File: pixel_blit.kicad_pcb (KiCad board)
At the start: 4 copper layers, 197.5 x 122 mm, 269 parts, among them CN1 PJ-3059-B, J1 DBT50G-9.5-2P, J10 DB301V-3.5-3P-GN, J11 DB301V-3.5-3P-GN, J12 DB301V-3.5-3P-GN, J13 DB301V-3.5-3P-GN, J14 DB301V-3.5-3P-GN, J15 DB301V-3.5-3P-GN, J16 DB301V-3.5-3P-GN, J17 DB301V-3.5-3P-GN, J18 DB301V-3.5-3P-GN, J19 DB301V-3.5-3P-GN, J2 DBT50G-9.5-2P, J20 DB301V-3.5-3P-GN, J21 DB301V-3.5-3P-GN, J22 DB301V-3.5-3P-GN, J23 DB301V-3.5-3P-GN, J24 DB301V-3.5-3P-GN, J25 DB301V-3.5-3P-GN, J26 DB301V-3.5-3P-GN, J27 DB301V-3.5-3P-GN, J28 DB301V-3.5-3P-GN, J29 DB301V-3.5-3P-GN, J3 DBT50G-9.5-2P, J30 DB301V-3.5-3P-GN, J31 DB301V-3.5-3P-GN, J32 DB301V-3.5-3P-GN, J33 DB301V-3.5-3P-GN, J34 DB301V-3.5-3P-GN, J35 DB301V-3.5-3P-GN, J36 DB301V-3.5-3P-GN, J37 Conn_01x03_Pin, J38 2.54-1*4, J4 DBT50G-9.5-2P, J5 DB301V-3.5-3P-GN, J6 DB301V-3.5-3P-GN, J7 DB301V-3.5-3P-GN, J8 DB301V-3.5-3P-GN, J9 DB301V-3.5-3P-GN, SW1 K2-1808SN-A4SW, SW2 SS-22D03-G040, U1 RP2350B_C42415655, U10 APS6404L-3SQR-SN, U2 W25Q128JVSIQTR, U3 TPS552872, U4 TPS62A02A, U5 SN74LVC8T245PWR, U6 SN74LVC8T245PWR, U7 SN74LVC8T245PWR, U8 SN74LVC8T245PWR, U9 RMC20452T

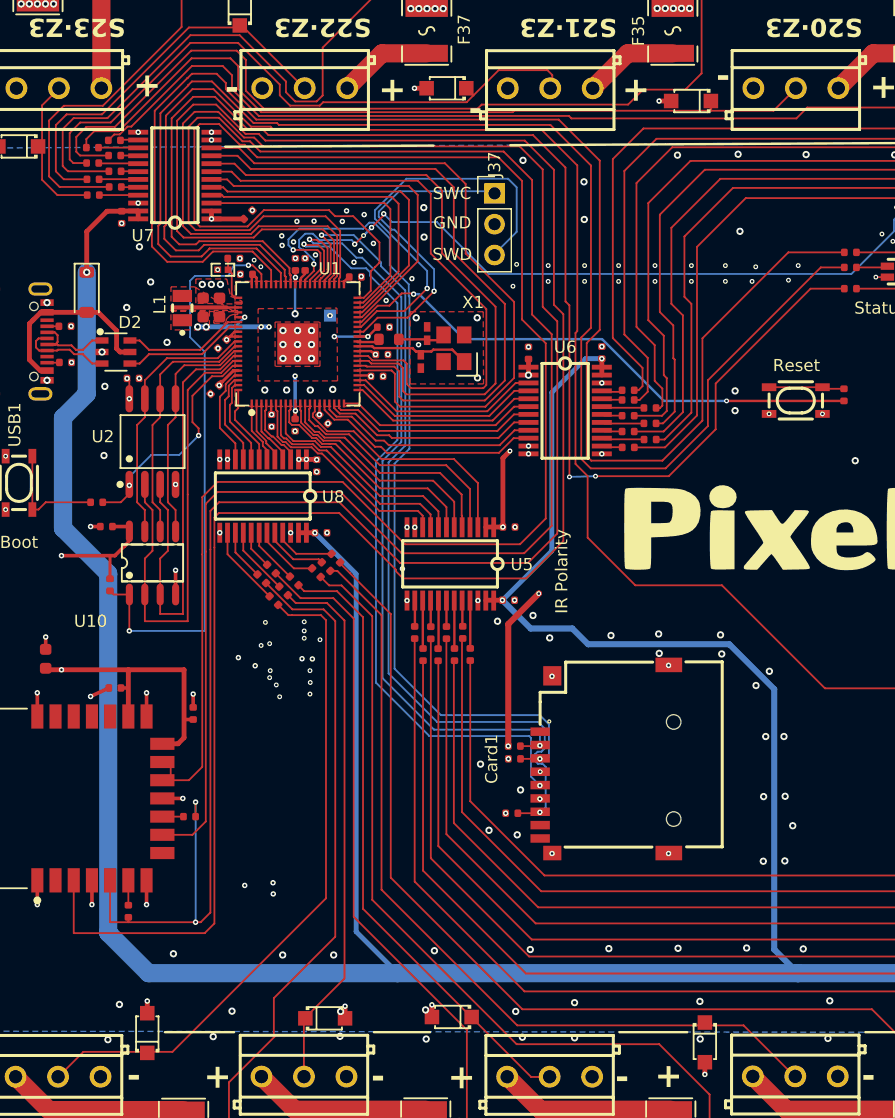
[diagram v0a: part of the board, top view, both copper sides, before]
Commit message: Reroute Wi-Fi lanes off SD_MOSI, add 33 ohm series resistor R75 on WL_CLK
The user's In2 reroute shortens the RM2 SPI lines from 147-173 mm to 70-85 mm.
Audit item 2 marked done; README resistor count updated.
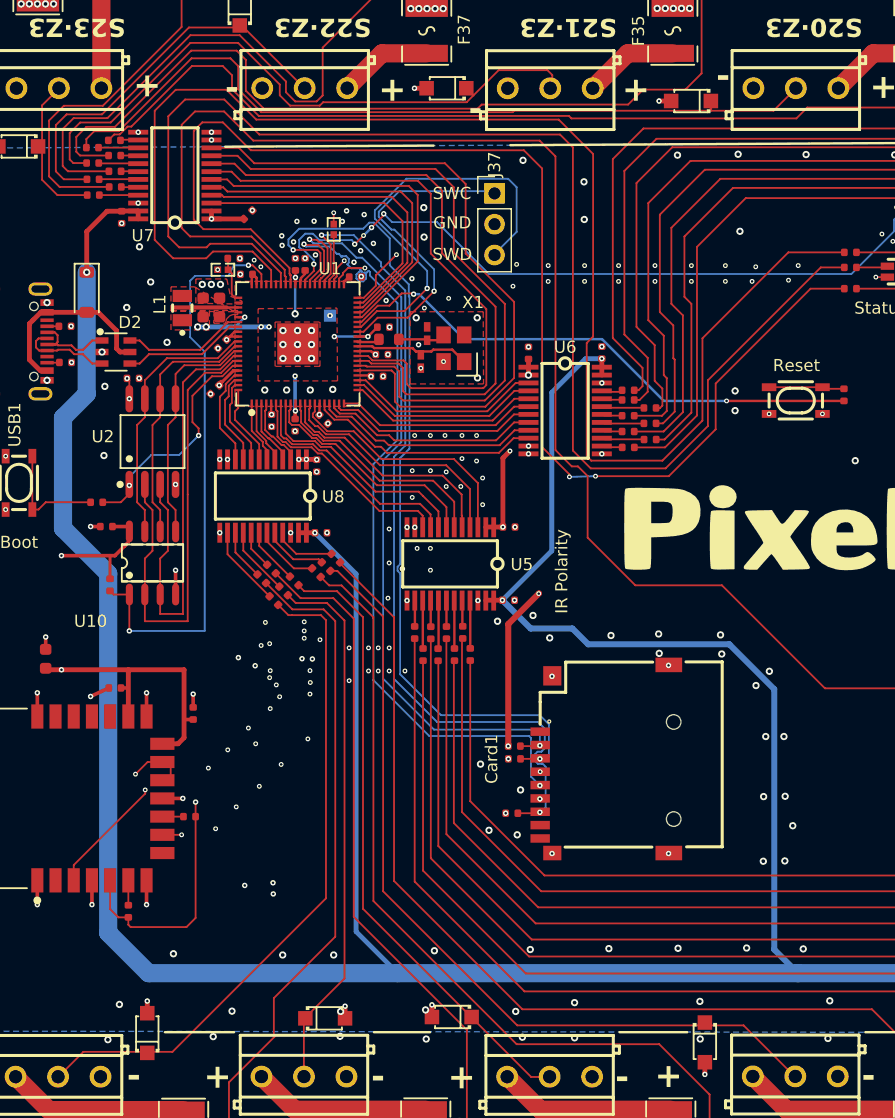
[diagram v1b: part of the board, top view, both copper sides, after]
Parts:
- added R75: 33Ω, PixelBlit:R0402, F.Cu at (82.9, 63.1)
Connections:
- U1 pad 44: WL_CLK -> Net-(U1-GPIO35)
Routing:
- net WL_CLK: track 173.6 -> 78.8 mm, vias 0 -> 2
- net WL_DATA: track 177.2 -> 85.0 mm
- net WL_CS: track 148.1 -> 70.3 mm, vias 0 -> 2
- net WL_ON: track 147.3 -> 82.7 mm, vias 0 -> 2
- net /LED_B: track 114.6 -> 106.4 mm
- net IR_IN: track 172.6 -> 166.5 mm
- net /LED_R: track 118.4 -> 114.2 mm
- net Net-(U1-GPIO35): track 0.00 -> 4.24 mm
- net SD_SCK: track 65.9 -> 69.1 mm
- net /LED_G: track 122.2 -> 119.5 mm
- net STRING23: track 24.1 -> 24.9 mm
- net STRING31: track 25.9 -> 26.5 mm
- net GND: vias 339 -> 383

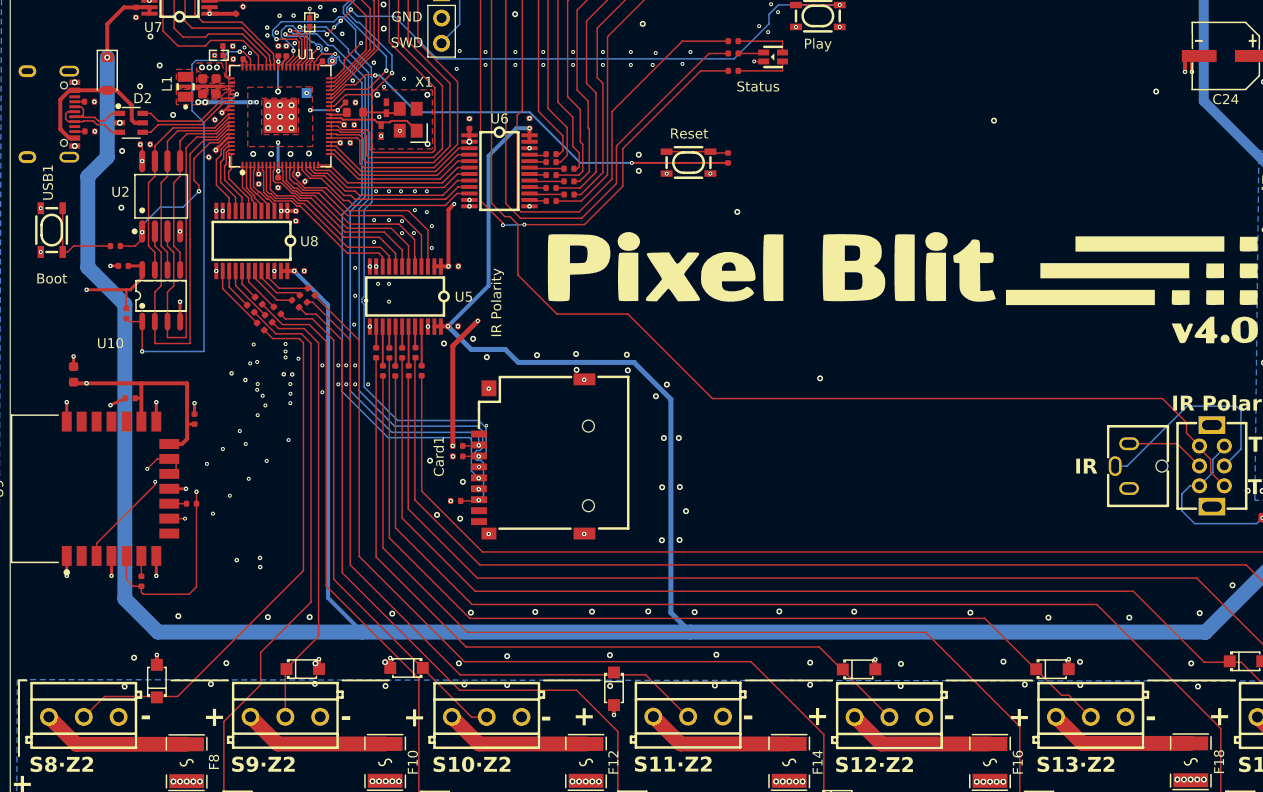
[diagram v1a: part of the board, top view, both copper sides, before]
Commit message: Widen the 3.3 V In2 trunk to 4 mm, 1 mm feed and triple via to the RM2
Stitching vias along the trunk moved out for clearance (three removed).
L3 to U1 drops from about 200 to 58 mOhm. Audit item 4 marked done.
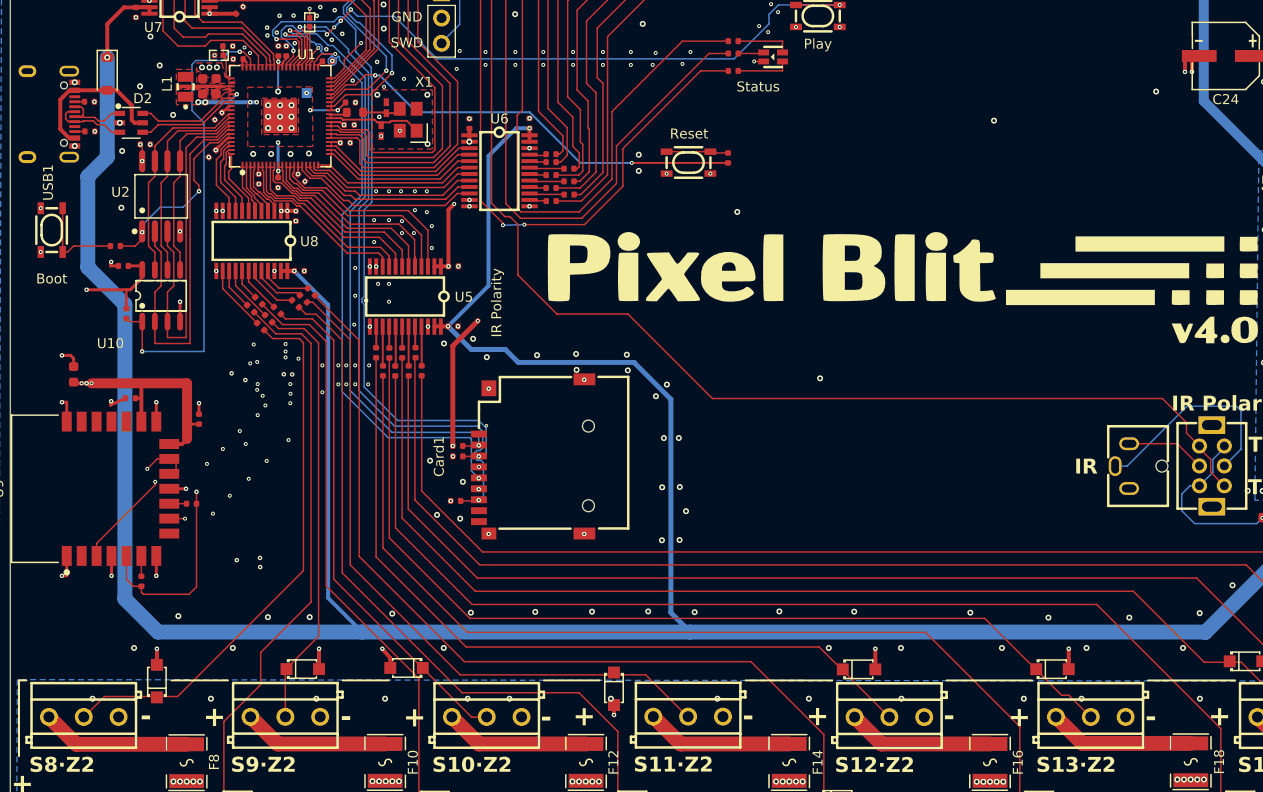
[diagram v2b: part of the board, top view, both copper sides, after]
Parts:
- moved C44 0.45 mm to (71.8, 103.0)
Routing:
- net GND: track 77.3 -> 85.2 mm, vias 383 -> 379
- net +3V3: vias 30 -> 32

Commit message: Clamp IR_IN at the jack: 1k series resistor R76 and B5819W to +3V3 (D51)
SW2's IR pins become IR_RAW; GPIO42 is an ADC pin and not 5 V tolerant.
Audit item 3 marked done; README part counts updated.
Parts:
- added D51: B5819W, PixelBlit:D_SOD-123, F.Cu at (164.0, 98.4)
- added R76: 1kΩ, PixelBlit:R_0402, F.Cu at (166.2, 100.9)
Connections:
- SW2 pad 3: IR_IN -> /Peripherals/IR_RAW
- SW2 pad 4: IR_IN -> /Peripherals/IR_RAW
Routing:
- net +3V3: track 403.1 -> 421.9 mm, vias 32 -> 33
- net IR_IN: track 166.5 -> 153.1 mm
- net /Peripherals/IR_RAW: track 0.00 -> 13.3 mm
